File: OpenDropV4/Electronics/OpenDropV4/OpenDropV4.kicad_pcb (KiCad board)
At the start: 2 copper layers, 124 x 115.4 mm, 159 parts, among them J1 USB_C_Receptacle, J2 Conn_02x05_Odd_Even, J3 Conn_01x24_Female, P1 CONN_01X01, P12 CONN_01X01, P13 ScrewPad1, P14 ScrewPad2, P15 ScrewPad3, P16 ScrewPad4, P2 ScrewPad4, P3 CONN_01X01, P7 CONN_01X01, SW1 SW_PUSH, SW2 SW_PUSH, SW3 SW_PUSH, SW5 SPST, T1 TK560P60Y, U1 MAX1771ESA, U10 AQY210EH, U11 AQY210EH, U12 AQY210EH, U13 AQY210EH, U14 TLV1117-33, U15 MCP41010, U16 74xx14, U3 PAM8301, U5 SAMD21G18B-A changed from SAM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, U6 MCP6002, U7 ACPL-024L-000E, U8 ACPL-024L-000E, U9 ACPL-024L-000E, Y1 32.765

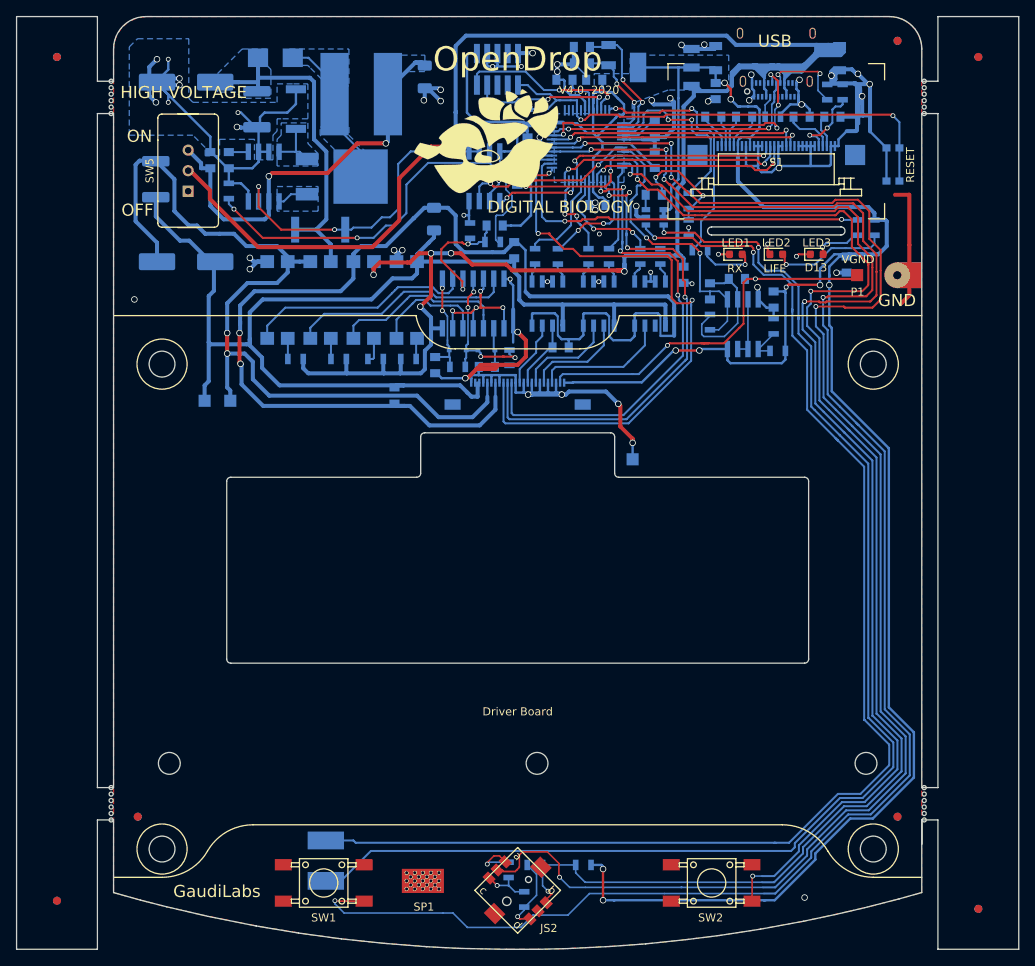
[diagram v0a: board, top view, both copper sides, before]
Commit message: Updated to V4.1 in Software and Electronics
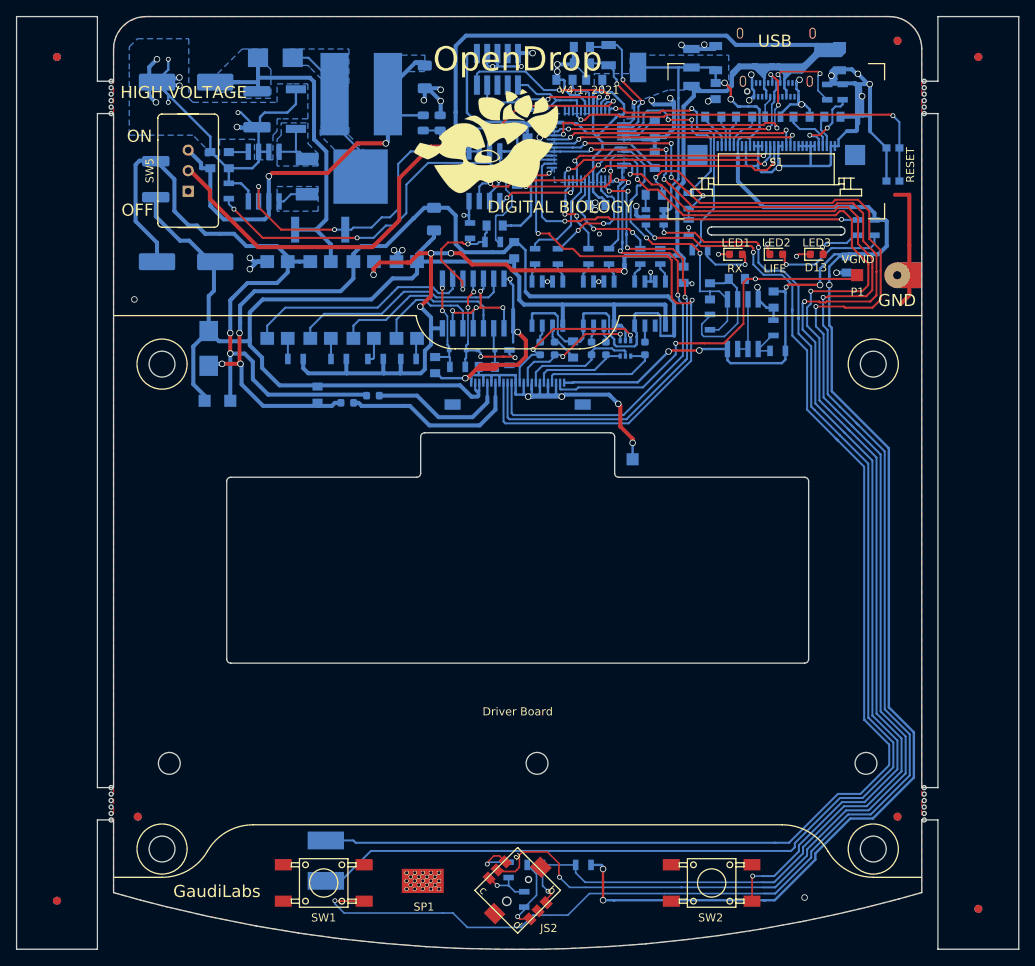
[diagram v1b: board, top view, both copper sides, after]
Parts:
- added D4: PESD5V0L5UY, Package_TO_SOT_SMD:SOT-363_SC-70-6, B.Cu at (113.3, 72.1)
- added D5: D_TVS, GaudiLabsFootPrints:DO-214AA, B.Cu at (61.8, 72.1)
- added FB1: Ferrite_Bead_Small, Inductor_SMD:L_0603_1608Metric, B.Cu at (102.8, 72.1)
- added FB2: Ferrite_Bead_Small, Inductor_SMD:L_0603_1608Metric, B.Cu at (109.1, 72.1)
- added FB3: Ferrite_Bead_Small, Inductor_SMD:L_0603_1608Metric, B.Cu at (104.6, 72.1)
- added FB4: Ferrite_Bead_Small, Inductor_SMD:L_0603_1608Metric, B.Cu at (110.9, 72.1)
- added FB5: Ferrite_Bead_Small, Inductor_SMD:L_0603_1608Metric, B.Cu at (115.7, 72.1)
- added FB6: Ferrite_Bead_Small, Inductor_SMD:L_0603_1608Metric, B.Cu at (78.9, 78.8)
- added FB8: Ferrite_Bead_Small, Inductor_SMD:L_0603_1608Metric, B.Cu at (82.1, 77.9)
- added R14: 10k, Resistor_SMD:R_0805_2012Metric, B.Cu at (90.4, 44.2)
- added R7: 6.8k, Resistor_SMD:R_0805_2012Metric, B.Cu at (88.3, 44.2)
- moved C13 9.53 mm to (75.2, 77.8)
- moved C37 1.56 mm to (106.9, 72.2), turned to 270 degrees
- moved R30 0.20 mm to (131.7, 69.5)
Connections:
- C37 pad 2: LE_C -> Net-(C37-Pad2)
- J3 pad 18: VDD_C -> Net-(FB6-Pad1)
- J3 pad 20: V_HV_C -> Net-(FB8-Pad1)
- U5 pad 13: LE -> DIG1
- U5 pad 15: DIG1 -> LE
- U5 pad 47: (no net) -> V_USB_SENS
- U7 pad 6: LE_C -> Net-(C37-Pad2)
- U7 pad 7: CLK_C -> Net-(FB1-Pad2)
- U8 pad 6: BL_C -> Net-(FB4-Pad2)
- U8 pad 7: POL_C -> Net-(FB2-Pad2)
- U9 pad 7: DI_C -> Net-(FB5-Pad2)
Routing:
- net V_USB_SENS: track 0.00 -> 28.6 mm, vias 0 -> 2
- net Net-(FB6-Pad1): track 0.00 -> 22.8 mm
- net V_HV_C: track 105.7 -> 85.4 mm
- net VDD_C: track 158.9 -> 139.3 mm, vias 2 -> 3
- net Net-(FB8-Pad1): track 0.00 -> 17.9 mm
- net CLK_C: track 8.55 -> 20.4 mm, vias 0 -> 2
- net LE_C: track 8.64 -> 16.2 mm, vias 0 -> 2
- net Net-(C1-Pad1): track 52.3 -> 58.8 mm
- net GND_C: track 147.7 -> 153.6 mm
- net Net-(C37-Pad2): track 0.00 -> 5.43 mm
- net GND: track 357.9 -> 362.3 mm
- net POL_C: track 12.3 -> 15.0 mm
- net Net-(FB1-Pad2): track 0.00 -> 2.47 mm
- net Net-(FB2-Pad2): track 0.00 -> 2.20 mm
- net Net-(FB4-Pad2): track 0.00 -> 2.13 mm
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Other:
- outline, holes or cut-outs redrawn
- board text added: "V4.1, 2021"
- board text removed: "V4.0, 2020"
- board text removed: "VDD_C"
